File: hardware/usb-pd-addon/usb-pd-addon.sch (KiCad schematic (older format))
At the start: 68 parts, among them J1 Conn_02x10_Odd_Even, J2 Conn_02x10_Odd_Even, J3 USB_TYPE_C, J4 Conn_02x05_Odd_Even, J5 Conn_02x05_Odd_Even, J6 EXT, J7 TP1, J8 TP2, J9 TP3, U1 FUSB302B, U2 AP2171W, U3 SN74AVC1T45DBVR, U4 SN74AVC1T45DBVR, U5 SN74AVC1T45DBVR, U6 SN74AVC1T45DBVR, U7 AP2127K-ADJ, U8 AP2127K-ADJ

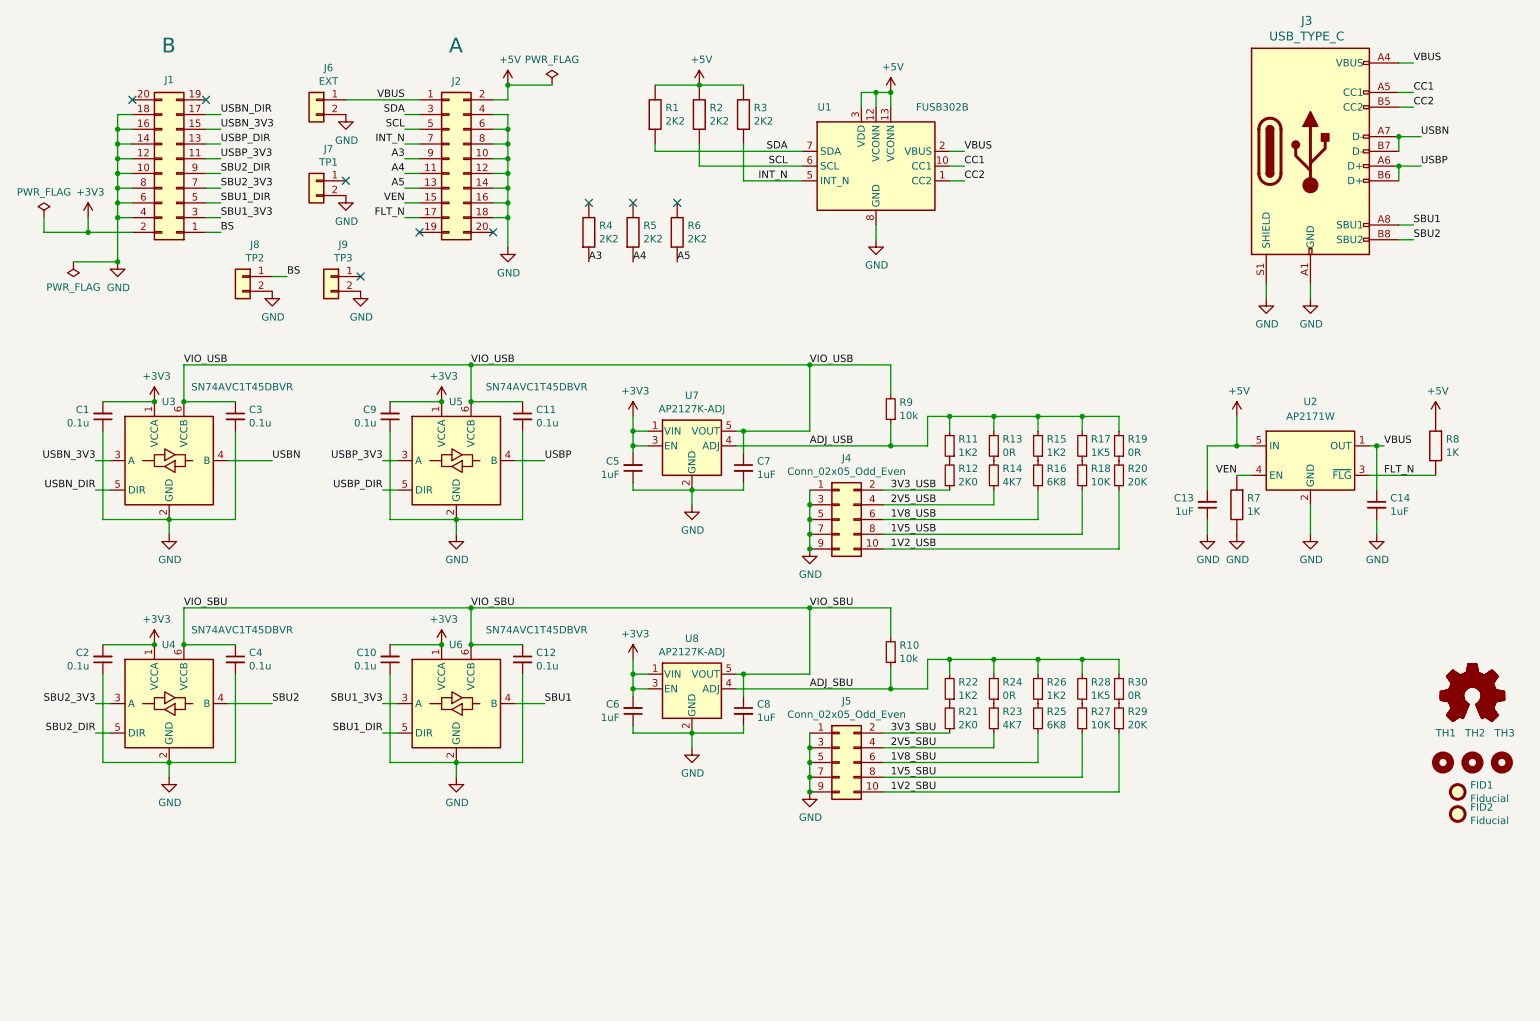
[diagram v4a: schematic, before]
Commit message: Corrected D+ pullup circuitry and added bypass cap.
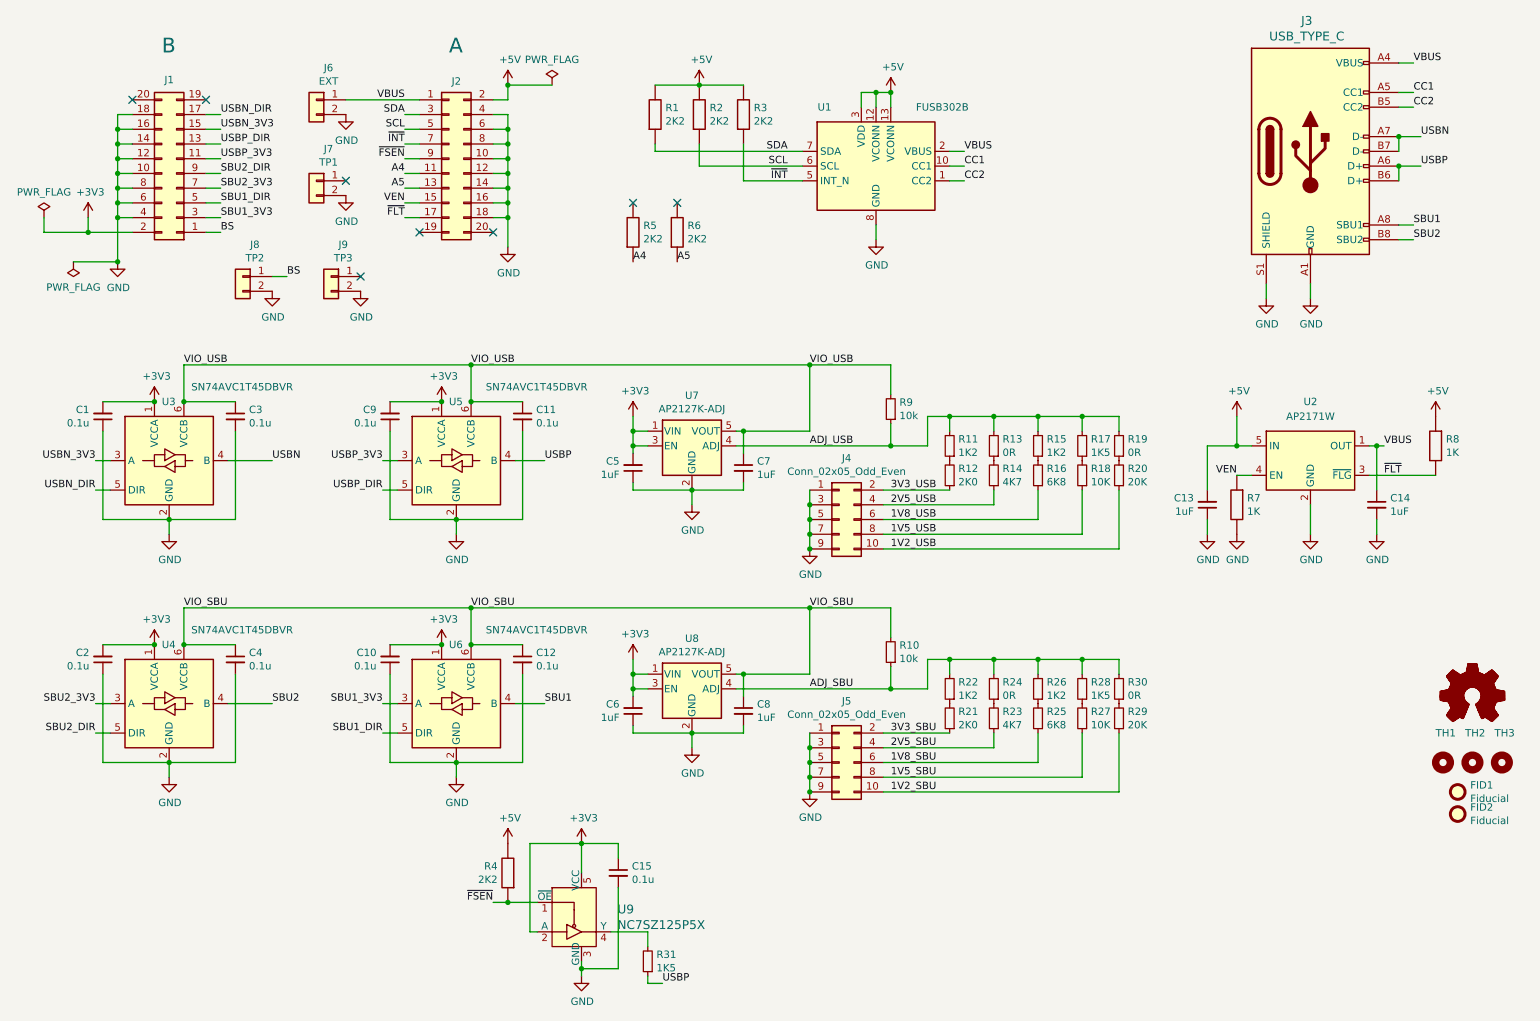
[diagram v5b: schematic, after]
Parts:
- added C15: 0.1u, pkl_dipol:C_0603, symbol Device:C_Small
- added R31: 1K5, pkl_dipol:R_0603, symbol pkl_device:pkl_R_Small
- added U9: NC7SZ125P5X, Package_TO_SOT_SMD:SOT-353_SC-70-5, symbol usb-pd-addon-rescue:NC7SZ125P5X-dk_Logic-Buffers-Drivers-Receivers-Transceivers
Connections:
- net +3V3: now also C15.1, U9.2 (A), U9.5 (VCC)
- net +5V: now also R4.1
- net GND: now also C15.2, U9.3 (GND)
- net USBP: now also R31.1
- net A3 renamed ~FSEN
- net ~FSEN: now also U9.1 (~OE)
- net FLT_N renamed ~FLT
- net INT_N renamed ~INT
- new net: R31.2, U9.4 (Y)
- no-connect marks 9 -> 8
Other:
- moved on the sheet: R4
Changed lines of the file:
@@
 Text Label 2100 1950 0    50   ~ 0
 USBP_3V3
-Text Label 2100 1850 0    50   ~ 0
-USBP_DIR
-Text Label 2100 1650 0    50   ~ 0
-USBN_DIR
 Text Label 3350 2350 2    50   ~ 0
-FLT_N
+~FLT
 Text Label 3350 2250 2    50   ~ 0
 VEN
 Text Label 3350 1850 2    50   ~ 0
-INT_N
+~INT
 Text Label 3350 1750 2    50   ~ 0
 SCL
@@
 SCL
 Text Label 5950 2100 2    50   ~ 0
-INT_N
+~INT
 Wire Wire Line
 	7050 1900 7150 1900
@@
 $EndComp
 Text Label 10000 4100 0    50   ~ 0
-FLT_N
+~FLT
 $Comp
 L pkl_device:pkl_R R8
@@
 Text Label 2100 2150 0    50   ~ 0
 SBU2_3V3
-Text Label 2100 2250 0    50   ~ 0
-SBU1_DIR
-Text Label 2100 2050 0    50   ~ 0
-SBU2_DIR
 $Comp
 L power:+3V3 #PWR018
@@
 L pkl_device:pkl_R R4
 U 1 1 6043A2B7
-P 4600 2450
-F 0 "R4" H 4670 2496 50  0000 L CNN
-F 1 "2K2" H 4670 2405 50  0000 L CNN
-F 2 "pkl_dipol:R_0603" V 4530 2450 30  0001 C CNN
-F 3 "" H 4600 2450 30  0000 C CNN
-F 4 "C4190" H 4600 2450 50  0001 C CNN "LCSC"
-	1    4600 2450
-	1    0    0    -1
+P 4050 6800
+F 0 "R4" H 4120 6846 50  0000 L CNN
+F 1 "2K2" H 4120 6755 50  0000 L CNN
+F 2 "pkl_dipol:R_0603" V 3980 6800 30  0001 C CNN
+F 3 "" H 4050 6800 30  0000 C CNN
+F 4 "C4190" H 4050 6800 50  0001 C CNN "LCSC"
+	1    4050 6800
+	-1   0    0    -1
 $EndComp
 $Comp
@@
 	1    0    0    -1
 $EndComp
-Text Label 3350 1950 2    50   ~ 0
-A3
+Text Label 3350 2150 2    50   ~ 0
+A5
 Text Label 3350 2050 2    50   ~ 0
 A4
-Text Label 3350 2150 2    50   ~ 0
+Text Label 3350 1950 2    50   ~ 0
+~FSEN
+Text Label 5200 2650 0    50   ~ 0
 A5
-Text Label 4600 2650 0    50   ~ 0
-A3
 Text Label 4900 2650 0    50   ~ 0
 A4
-Text Label 5200 2650 0    50   ~ 0
-A5
 Wire Wire Line
 	7650 4400 7650 4200
@@
 Text Label 6100 5550 0    50   ~ 0
 ADJ_SBU
-NoConn ~ 4600 2250
+NoConn ~ 5200 2250
 NoConn ~ 4900 2250
-NoConn ~ 5200 2250
 $Comp
 L pkl_device:pkl_R_Small R15
@@
 Wire Wire Line
 	9950 3900 10000 3900
+$Comp
+L pkl_device:pkl_R_Small R31
+U 1 1 6029F428
+P 5000 7400
+F 0 "R31" H 4941 7354 50  0000 R CNN
+F 1 "1K5" H 4941 7445 50  0000 R CNN
+F 2 "pkl_dipol:R_0603" V 4930 7400 50  0001 C CNN
+F 3 "https://datasheet.lcsc.com/szlcsc/Uniroyal-Elec-0603WAF1201T5E_C22765.pdf" V 5000 7400 50  0001 C CNN
+F 4 "C22843" V 5000 7400 50  0001 C CNN "LCSC"
+	1    5000 7400
+	-1   0    0    1
+$EndComp
+Wire Wire Line
+	5000 7500 5000 7550
+Wire Wire Line
+	5000 7550 5100 7550
+Text Label 5100 7550 0    50   ~ 0
+USBP
+$Comp
+L power:GND #PWR0112
+U 1 1 602DBD95
+P 4550 7500
+F 0 "#PWR0112" H 4550 7250 50  0001 C CNN
+F 1 "GND" H 4555 7327 50  0000 C CNN
+F 2 "" H 4550 7500 50  0001 C CNN
+F 3 "" H 4550 7500 50  0001 C CNN
+	1    4550 7500
+	1    0    0    -1
+$EndComp
+Text Label 3950 7000 2    50   ~ 0
+~FSEN
+Wire Wire Line
+	5000 7200 5000 7300
+Text Label 2100 2250 0    50   ~ 0
+SBU1_DIR
+Text Label 2100 2050 0    50   ~ 0
+SBU2_DIR
+Text Label 2100 1850 0    50   ~ 0
+USBP_DIR
+Text Label 2100 1650 0    50   ~ 0
+USBN_DIR
+$Comp
+L usb-pd-addon-rescue:NC7SZ125P5X-dk_Logic-Buffers-Drivers-Receivers-Transceivers U9
+U 1 1 60278052
+P 4550 7100
+F 0 "U9" H 4794 7153 60  0000 L CNN
+F 1 "NC7SZ125P5X" H 4794 7047 60  0000 L CNN
+F 2 "Package_TO_SOT_SMD:SOT-353_SC-70-5" H 4750 7300 60  0001 L CNN
+F 3 "https://www.onsemi.com/pub/Collateral/NC7SZ125-D.PDF" H 4750 7400 60  0001 L CNN
+F 4 "NC7SZ125P5XCT-ND" H 4750 7500 60  0001 L CNN "Digi-Key_PN"
+F 5 "NC7SZ125P5X" H 4750 7600 60  0001 L CNN "MPN"
+F 6 "Integrated Circuits (ICs)" H 4750 7700 60  0001 L CNN "Category"
+F 7 "Logic - Buffers, Drivers, Receivers, Transceivers" H 4750 7800 60  0001 L CNN "Family"
+F 8 "https://www.onsemi.com/pub/Collateral/NC7SZ125-D.PDF" H 4750 7900 60  0001 L CNN "DK_Datasheet_Link"
+F 9 "/product-detail/en/on-semiconductor/NC7SZ125P5X/NC7SZ125P5XCT-ND/673393" H 4750 8000 60  0001 L CNN "DK_Detail_Page"
+F 10 "IC BUF NON-INVERT 5.5V SC70-5" H 4750 8100 60  0001 L CNN "Description"
+F 11 "ON Semiconductor" H 4750 8200 60  0001 L CNN "Manufacturer"
+F 12 "Active" H 4750 8300 60  0001 L CNN "Status"
+	1    4550 7100
+	1    0    0    -1
+$EndComp
+Wire Wire Line
+	4550 6600 4550 6800
+$Comp
+L power:+3V3 #PWR023
+U 1 1 604FC608
+P 4550 6600
+F 0 "#PWR023" H 4550 6450 50  0001 C CNN
+F 1 "+3V3" H 4565 6773 50  0000 C CNN
+F 2 "" H 4550 6600 50  0001 C CNN
+F 3 "" H 4550 6600 50  0001 C CNN
+	1    4550 6600
+	1    0    0    -1
+$EndComp
+Connection ~ 4550 6600
+$Comp
+L Device:C_Small C15
+U 1 1 6051DD76
+P 4800 6800
+F 0 "C15" H 4892 6846 50  0000 L CNN
+F 1 "0.1u" H 4892 6755 50  0000 L CNN
+F 2 "pkl_dipol:C_0603" H 4800 6800 50  0001 C CNN
+F 3 "~" H 4800 6800 50  0001 C CNN
+F 4 "C14663" H 4800 6800 50  0001 C CNN "LCSC"
+	1    4800 6800
+	1    0    0    -1
+$EndComp
+Wire Wire Line
+	4750 7200 5000 7200
+Wire Wire Line
+	4800 6700 4800 6600
+Wire Wire Line
+	4800 6600 4550 6600
+Wire Wire Line
+	4550 7400 4550 7450
+Wire Wire Line
+	4800 7450 4550 7450
+Wire Wire Line
+	4800 6900 4800 7450
+Connection ~ 4550 7450
+Wire Wire Line
+	4550 7450 4550 7500
+Wire Wire Line
+	3950 7000 4050 7000
+Wire Wire Line
+	4250 7200 4200 7200
+Wire Wire Line
+	4200 7200 4200 6600
+Wire Wire Line
+	4200 6600 4550 6600
+Connection ~ 4050 7000
+Wire Wire Line
+	4050 7000 4250 7000
+$Comp
+L power:+5V #PWR0113
+U 1 1 60659740
+P 4050 6600
+F 0 "#PWR0113" H 4050 6450 50  0001 C CNN
+F 1 "+5V" H 4065 6773 50  0000 C CNN
+F 2 "" H 4050 6600 50  0001 C CNN
+F 3 "" H 4050 6600 50  0001 C CNN
+	1    4050 6600
+	1    0    0    -1
+$EndComp
 $EndSCHEMATC

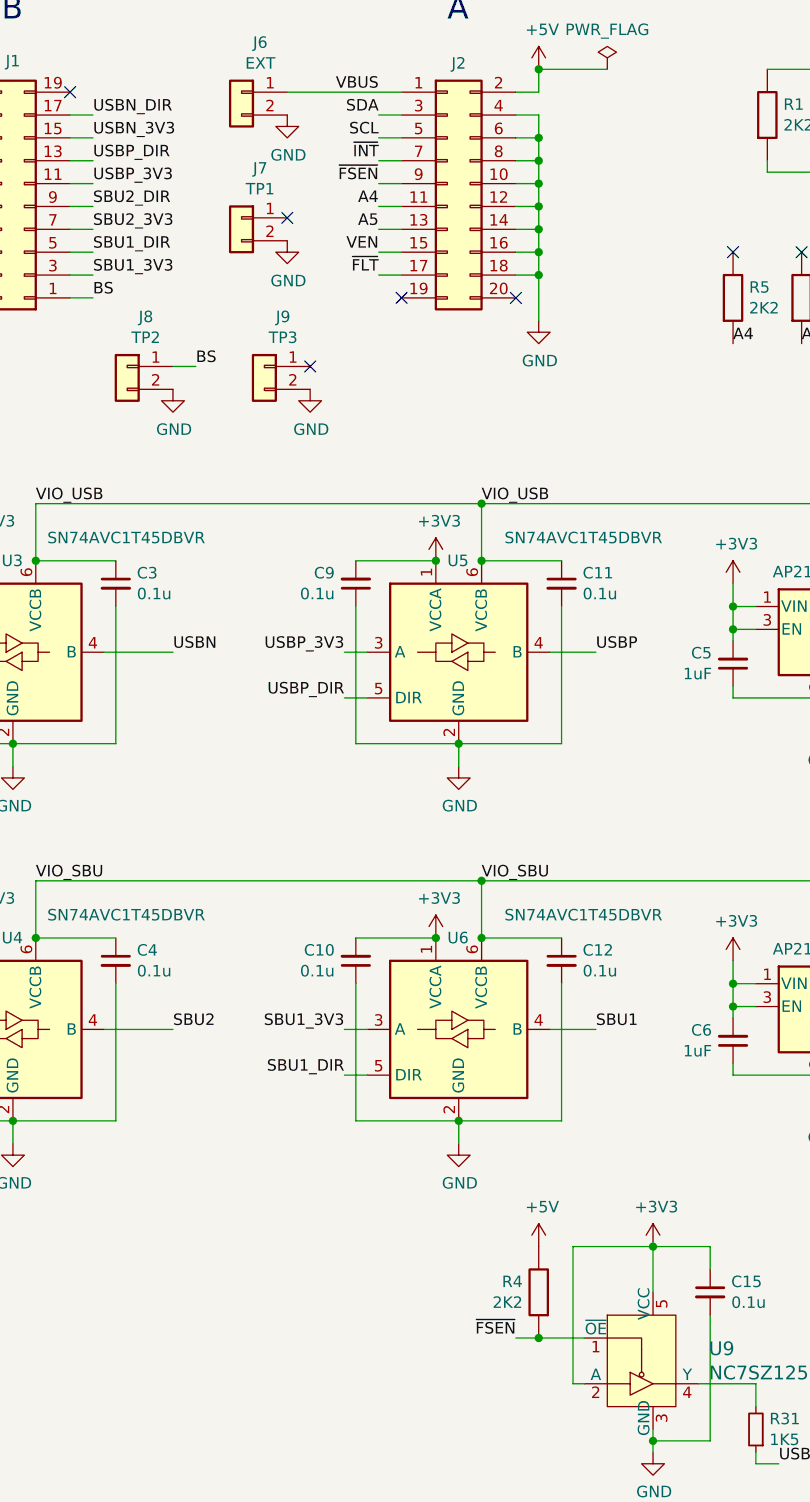
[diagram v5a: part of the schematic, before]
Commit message: Better mnemonic for the FS pull-up switch enable.
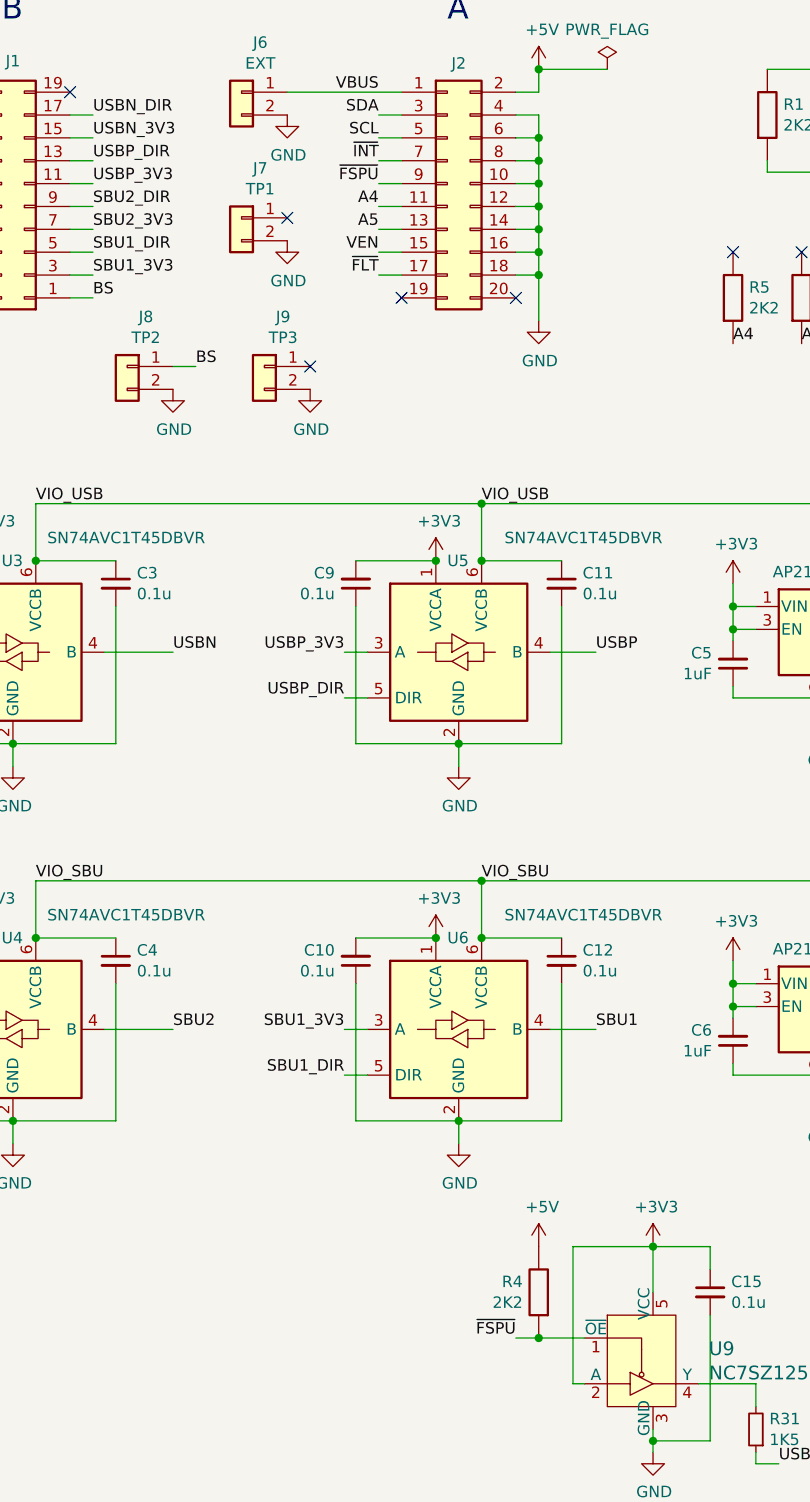
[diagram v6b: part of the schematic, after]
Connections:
- net ~FSEN renamed ~FSPU
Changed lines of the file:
@@
 A4
 Text Label 3350 1950 2    50   ~ 0
-~FSEN
+~FSPU
 Text Label 5200 2650 0    50   ~ 0
 A5
@@
 $EndComp
 Text Label 3950 7000 2    50   ~ 0
-~FSEN
+~FSPU
 Wire Wire Line
 	5000 7200 5000 7300
